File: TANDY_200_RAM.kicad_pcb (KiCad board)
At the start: 2 copper layers, 35.6 x 20.3 mm, 4 parts, among them J1 TANDY_26-3688, U1 62256_SOP28, U2 74LVC2G00

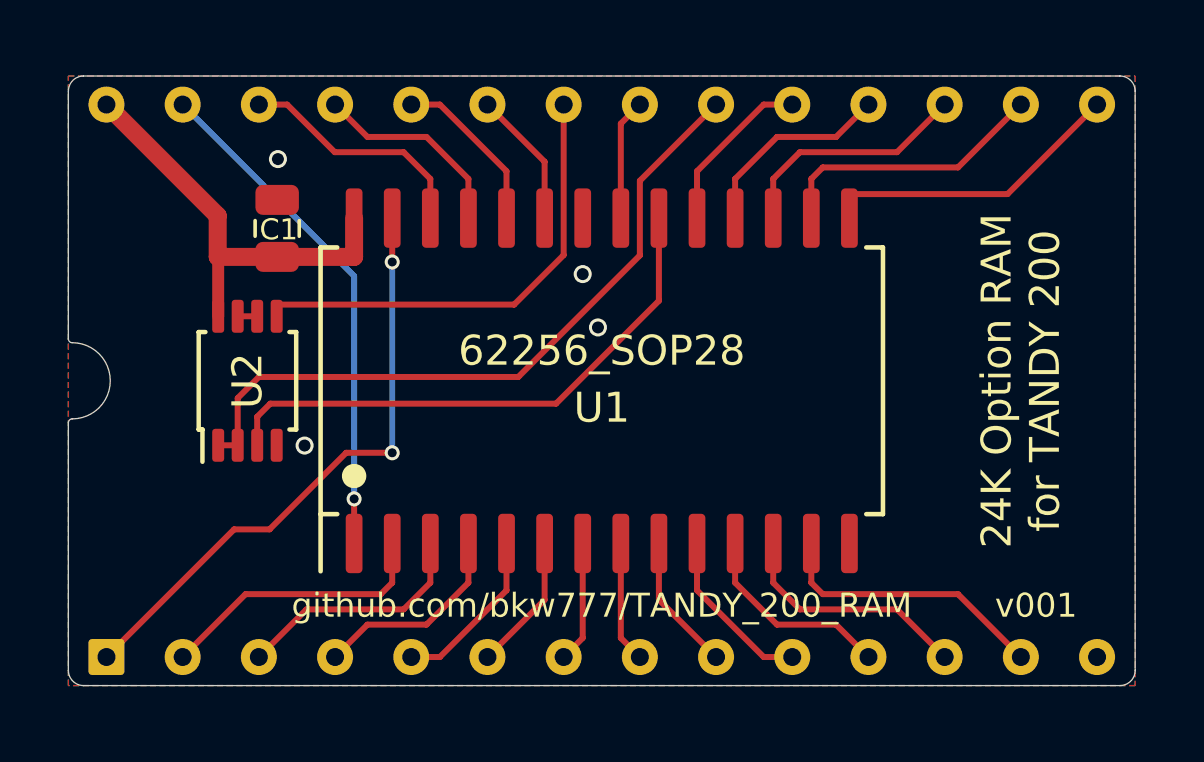
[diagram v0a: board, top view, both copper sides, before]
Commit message: board outlines, ground planes
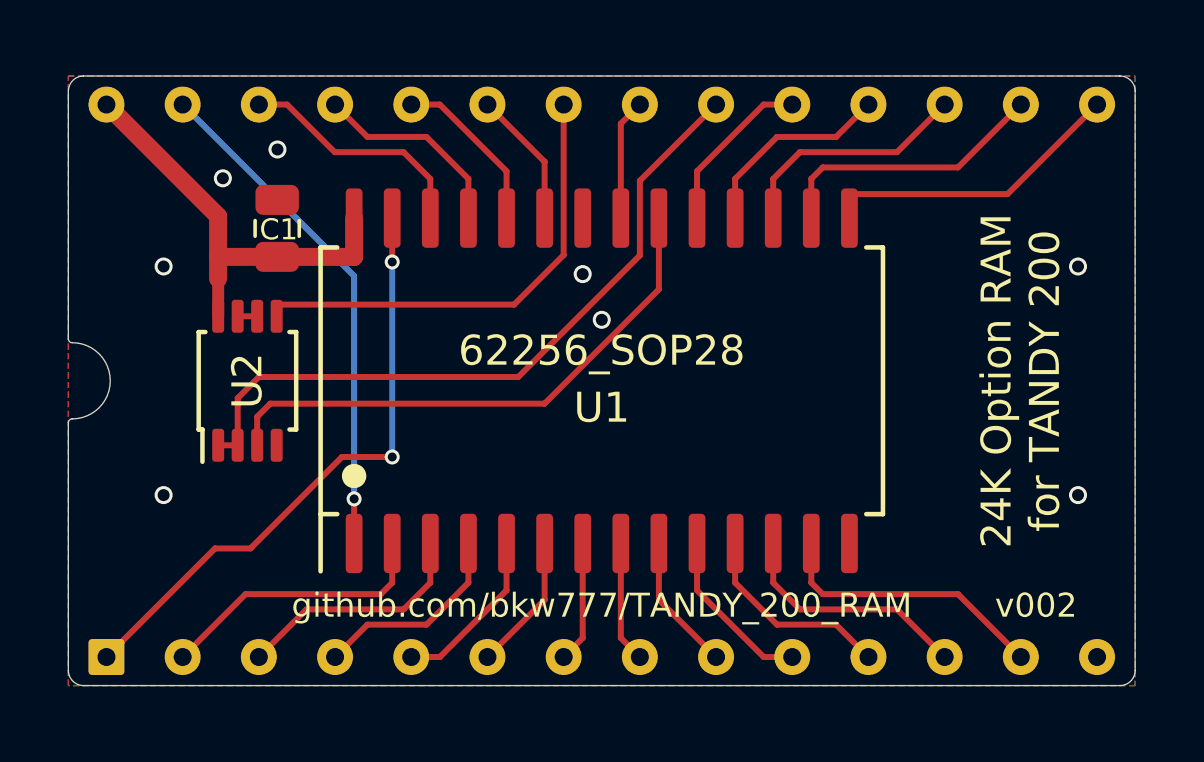
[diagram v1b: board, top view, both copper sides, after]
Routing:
- net VCC: track 15.8 -> 14.4 mm
- net GND: vias 4 -> 8
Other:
- board text removed: "Row spacing is 725mils, not 700."

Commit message: add single-bank tsop
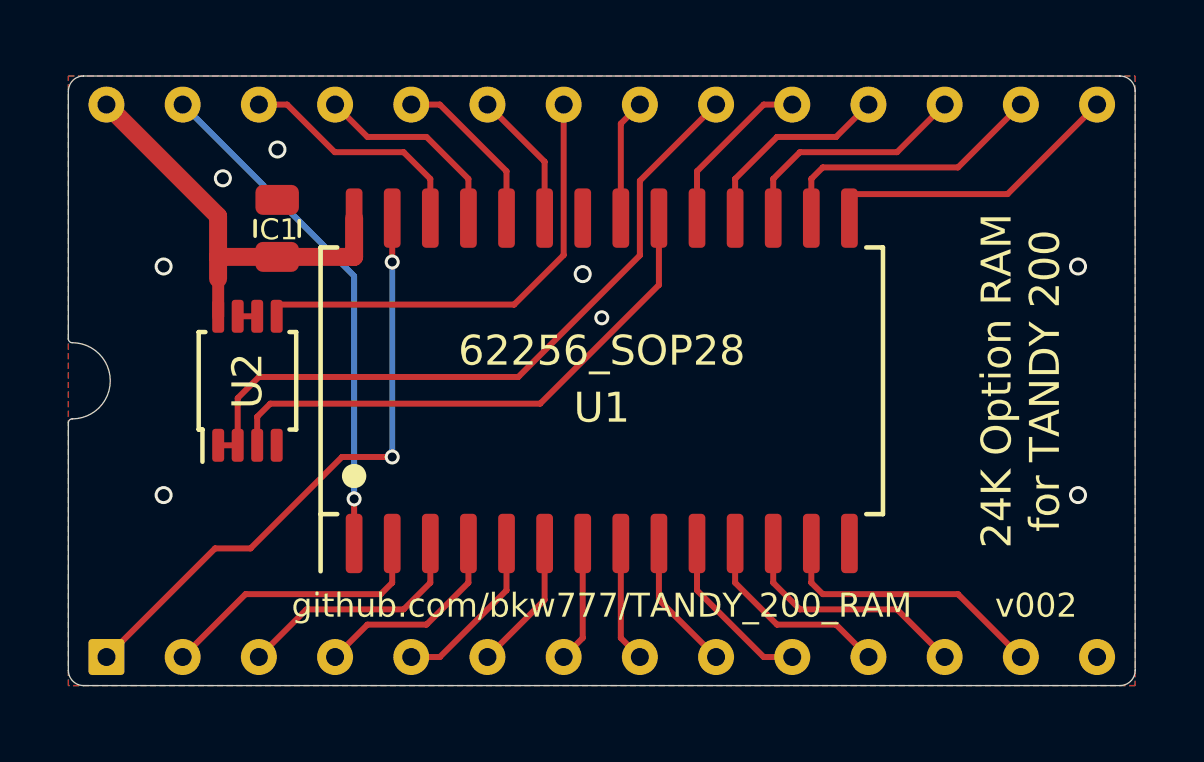
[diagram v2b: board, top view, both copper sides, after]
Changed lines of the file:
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@@
   (via (at 124.946 109.728) (size 0.6) (drill 0.4) (layers "F.Cu" "B.Cu") (free) (net 3))
   (via (at 124.946 102.108) (size 0.6) (drill 0.4) (layers "F.Cu" "B.Cu") (free) (net 3))
-  (via (at 139.551 103.886) (size 0.6) (drill 0.4) (layers "F.Cu" "B.Cu") (free) (net 3))
+  (via (at 139.551 103.818) (size 0.5) (drill 0.3) (layers "F.Cu" "B.Cu") (free) (net 3))
   (segment (start 146.536 111.3409) (end 146.536 112.649) (width 0.2) (layer "F.Cu") (net 4))
   (segment (start 146.917 113.03) (end 151.4255 113.03) (width 0.2) (layer "F.Cu") (net 4))
@@
   (segment (start 135.106 100.4951) (end 135.106 99.187) (width 0.2) (layer "F.Cu") (net 28))
   (segment (start 131.7405 97.79) (end 130.661 96.7105) (width 0.2) (layer "F.Cu") (net 28))
-  (segment (start 137.646 106.68) (end 128.502 106.68) (width 0.2) (layer "F.Cu") (net 29))
   (segment (start 128.065 107.117) (end 128.065 108.068) (width 0.2) (layer "F.Cu") (net 29))
-  (segment (start 141.456 102.87) (end 137.646 106.68) (width 0.2) (layer "F.Cu") (net 29))
-  (segment (start 141.456 100.4951) (end 141.456 102.87) (width 0.2) (layer "F.Cu") (net 29))
+  (segment (start 141.456 102.723) (end 137.499 106.68) (width 0.2) (layer "F.Cu") (net 29))
+  (segment (start 141.456 100.4951) (end 141.456 102.723) (width 0.2) (layer "F.Cu") (net 29))
   (segment (start 128.502 106.68) (end 128.065 107.117) (width 0.2) (layer "F.Cu") (net 29))
+  (segment (start 137.499 106.68) (end 128.502 106.68) (width 0.2) (layer "F.Cu") (net 29))
   (segment (start 127.415 103.768) (end 128.065 103.768) (width 0.2) (layer "F.Cu") (net 30))
   (zone (net 3) (net_name "GND") (layer "F.Cu") (hatch edge 0.508)

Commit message: ground paths, footprints, sch symbols
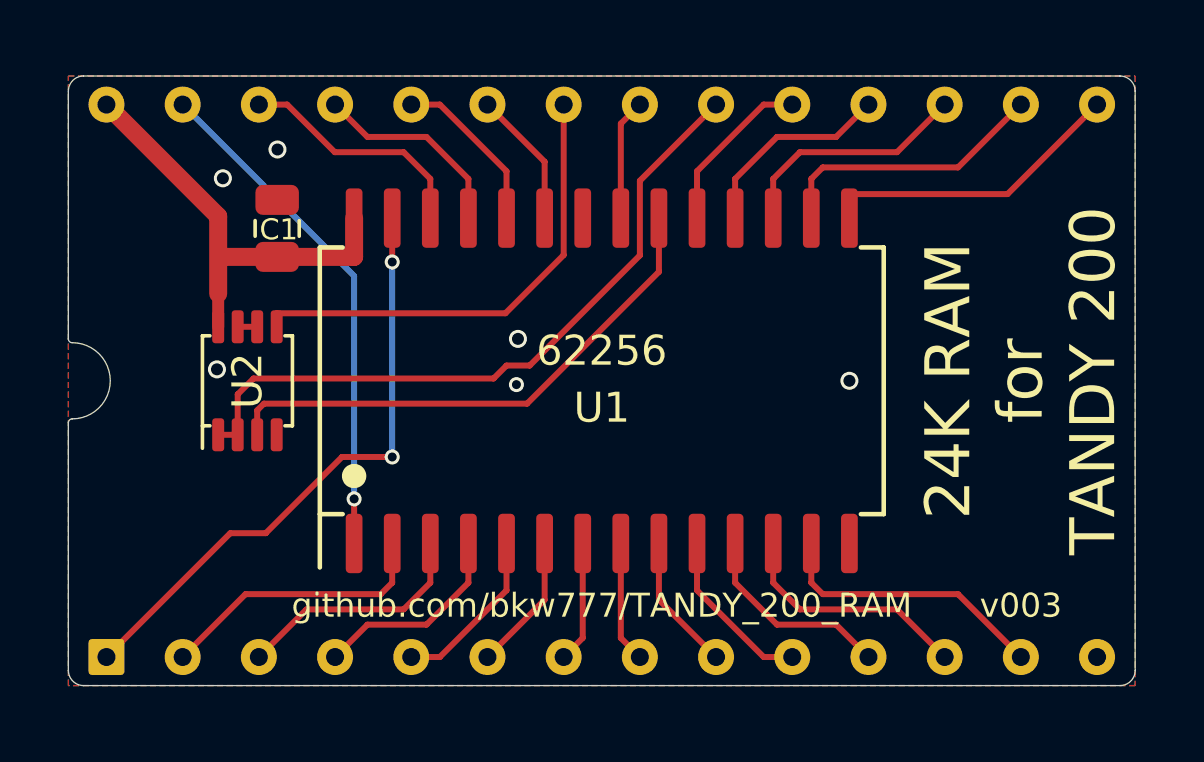
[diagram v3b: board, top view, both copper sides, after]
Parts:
- U1: value 62256_SOP28 -> 62256
- U2: footprint 000_LOCAL:SOT-505-2 -> 000_LOCAL:SSOP-8_2.95x2.8x0.65
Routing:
- net GND: vias 8 -> 6
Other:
- board text added: "24K RAM for TANDY 200"
- board text removed: "24K Option RAM for TANDY 200"

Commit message: 24k tsop layout and all board outlines expanded slightly
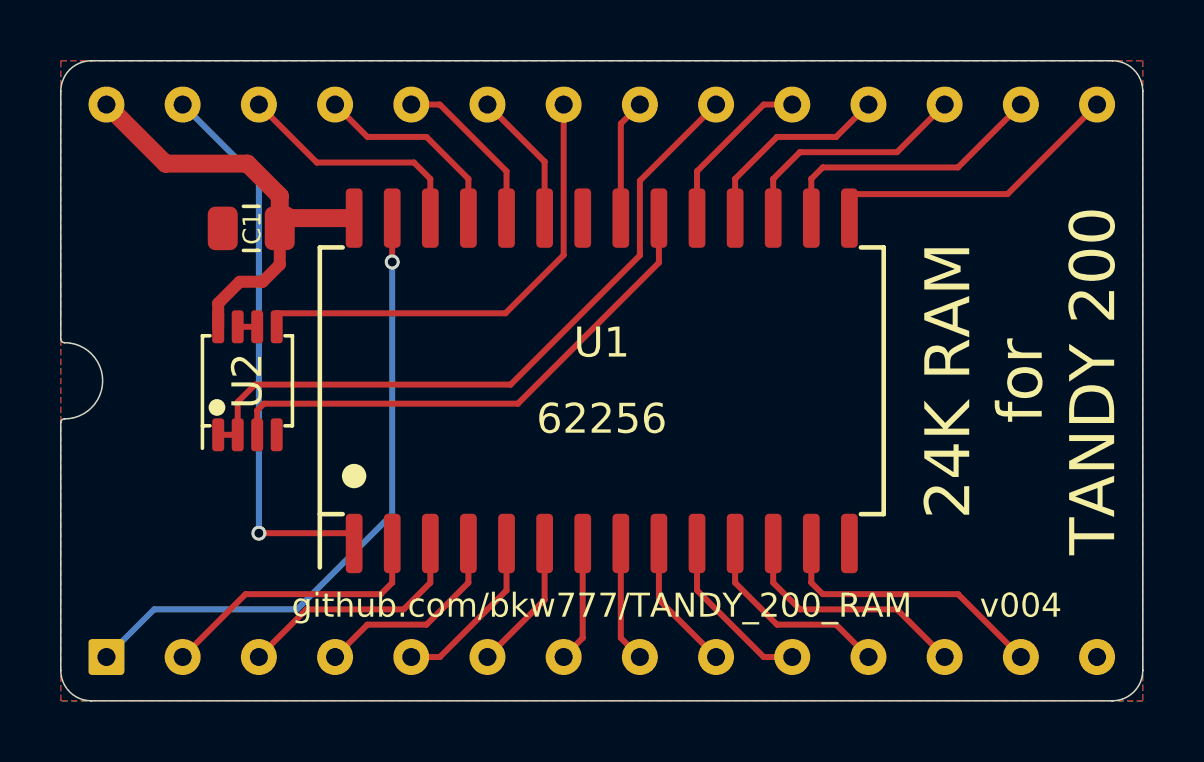
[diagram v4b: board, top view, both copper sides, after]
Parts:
- J1: footprint 000_LOCAL:KEL ICC05-028-360TP PCB -> 000_LOCAL:KEL ICC05-028-360TP
- moved C1 0.86 mm to (127.9, 100.8), turned to 180 degrees
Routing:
- net /A14: track 17.0 -> 18.9 mm
- net /~{WE}: track 20.2 -> 21.4 mm, vias 2 -> 1
- net VCC: track 14.7 -> 15.3 mm
- net GND: vias 6 -> 0
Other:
- board size 35.6 x 20.3 mm -> 36.1 x 21.3 mm
- board text added: "C1: ${f8b4e7cd-2ae3-4bf6-a8be-6993d42cff17:VALUE} U2: ${3470d911-901b-4b27-bf80-f5eb7fe37763:VALUE} LEGS: Mill-Max 3121 or TE 1544210"
- board text removed: "C1: 0.1uF U2: 74LVC2G00 LEGS: Mill-Max 3121 or TE 1544210"
